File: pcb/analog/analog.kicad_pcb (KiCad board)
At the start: 2 copper layers, 70 x 70 mm, 65 parts, among them J1 USB_C_Receptacle_USB2.0, SW1 SW_Push, SW2 SW_Push, U1 SRV05-4, U2 XC6206P332MR, U3 DRV5056A3xDBZxQ1, U4 DRV5056A3xDBZxQ1, U5 DRV5056A3xDBZxQ1, U6 74AHCT1G125, U7 74AHCT1G125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

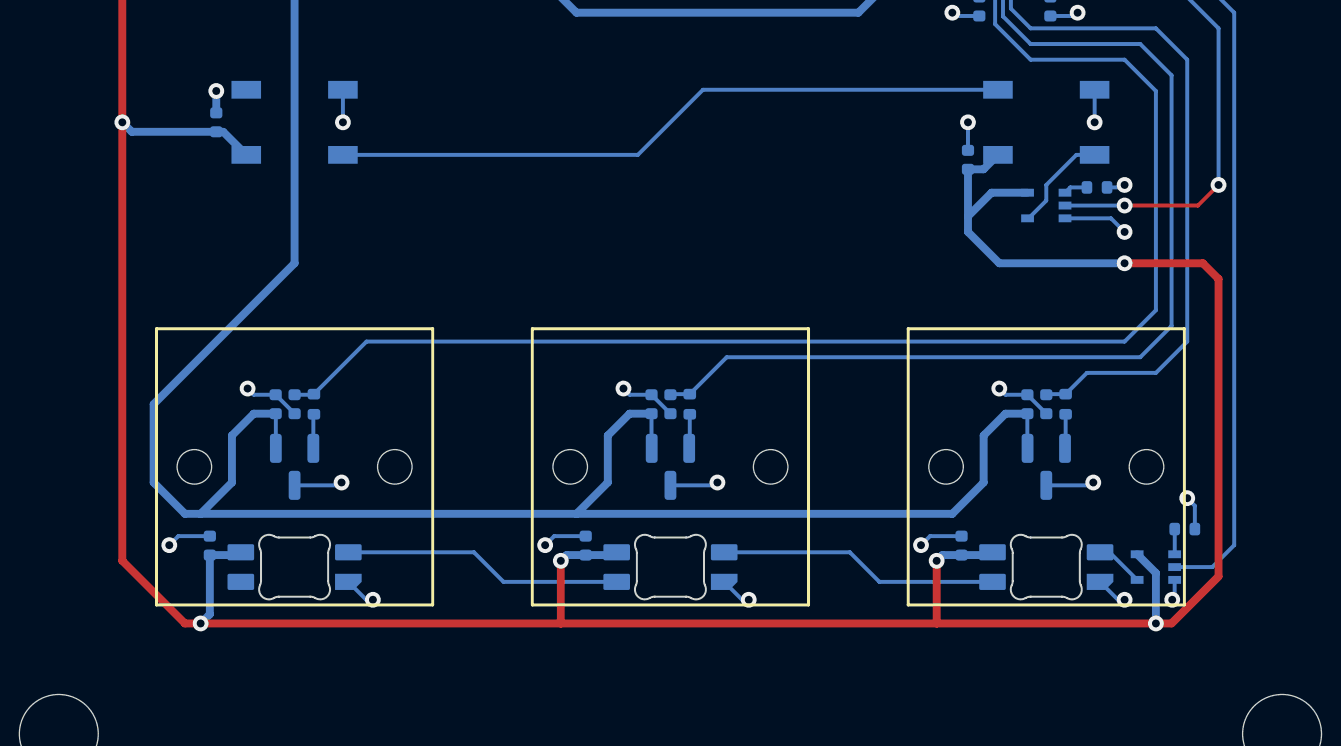
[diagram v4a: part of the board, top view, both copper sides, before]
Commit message: refactor: route +5v for underglow without crossing over analog lines
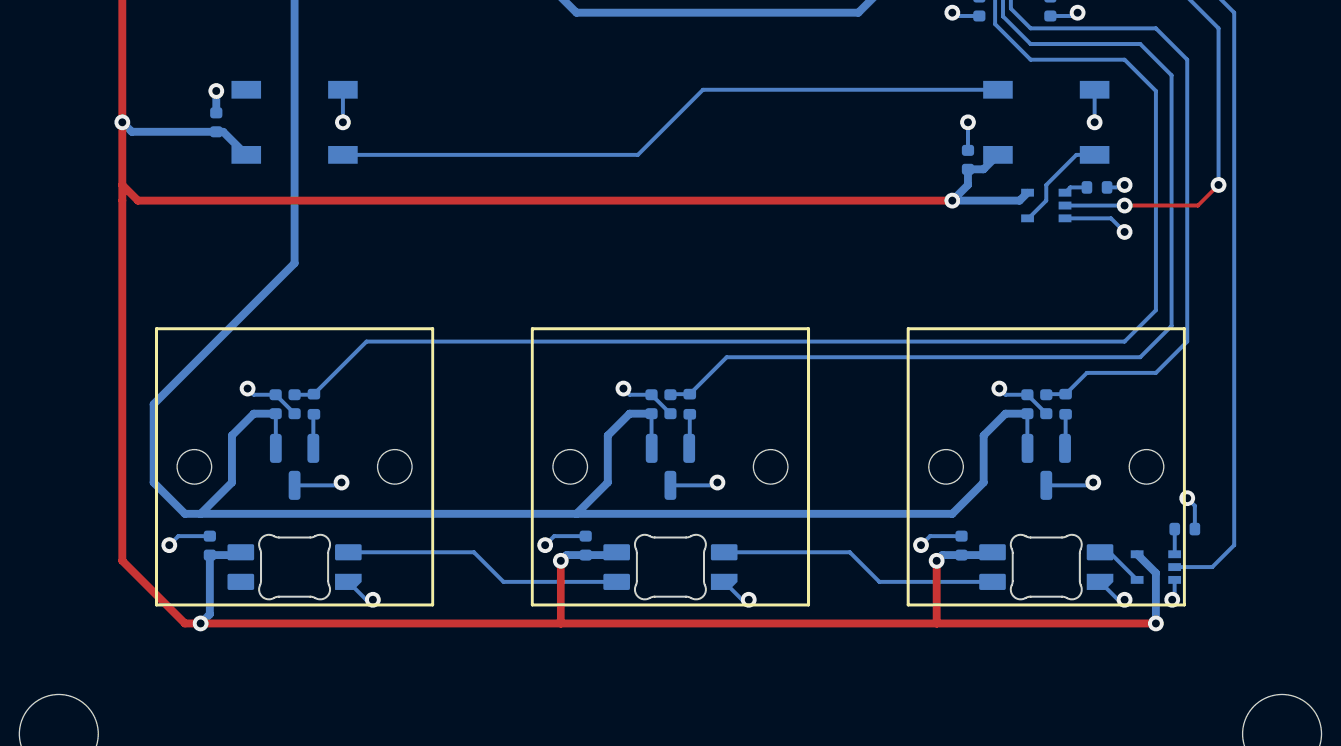
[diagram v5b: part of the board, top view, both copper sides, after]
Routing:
- net +5V: track 203.7 -> 212.3 mm
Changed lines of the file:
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@@
   (segment (start 76.670543 39.959446) (end 76.670543 40.93645) (width 0.2) (layer "B.Cu") (net 2))
   (segment (start 45.24375 76.2) (end 45.24375 73.025) (width 0.4) (layer "F.Cu") (net 3))
+  (segment (start 23.01875 54.76875) (end 23.01875 73.025) (width 0.4) (layer "F.Cu") (net 3))
   (segment (start 23.01875 29.36875) (end 23.01875 50.8) (width 0.4) (layer "F.Cu") (net 3))
-  (segment (start 23.01875 50.8) (end 23.01875 73.025) (width 0.4) (layer "F.Cu") (net 3))
-  (segment (start 77.7875 74.6125) (end 78.58125 73.81875) (width 0.4) (layer "F.Cu") (net 3))
   (segment (start 45.24375 76.2) (end 64.29375 76.2) (width 0.4) (layer "F.Cu") (net 3))
   (segment (start 23.01875 73.025) (end 26.19375 76.2) (width 0.4) (layer "F.Cu") (net 3))
   (segment (start 26.9875 76.2) (end 45.24375 76.2) (width 0.4) (layer "F.Cu") (net 3))
   (segment (start 26.19375 76.2) (end 26.9875 76.2) (width 0.4) (layer "F.Cu") (net 3))
+  (segment (start 23.01875 50.8) (end 23.01875 53.975) (width 0.4) (layer "F.Cu") (net 3))
   (segment (start 40.48125 25.4) (end 26.9875 25.4) (width 0.4) (layer "F.Cu") (net 3))
-  (segment (start 78.58125 73.81875) (end 78.58125 58.7375) (width 0.4) (layer "F.Cu") (net 3))
-  (segment (start 75.40625 76.2) (end 76.2 76.2) (width 0.4) (layer "F.Cu") (net 3))
-  (segment (start 77.7875 57.94375) (end 73.81875 57.94375) (width 0.4) (layer "F.Cu") (net 3))
+  (segment (start 23.8125 54.76875) (end 65.0875 54.76875) (width 0.4) (layer "F.Cu") (net 3))
+  (segment (start 23.01875 53.975) (end 23.01875 54.76875) (width 0.4) (layer "F.Cu") (net 3))
   (segment (start 26.9875 25.4) (end 23.01875 29.36875) (width 0.4) (layer "F.Cu") (net 3))
   (segment (start 64.29375 76.2) (end 75.40625 76.2) (width 0.4) (layer "F.Cu") (net 3))
-  (segment (start 76.2 76.2) (end 77.7875 74.6125) (width 0.4) (layer "F.Cu") (net 3))
+  (segment (start 23.01875 53.975) (end 23.8125 54.76875) (width 0.4) (layer "F.Cu") (net 3))
   (segment (start 64.29375 76.2) (end 64.29375 73.025) (width 0.4) (layer "F.Cu") (net 3))
-  (segment (start 78.58125 58.7375) (end 77.7875 57.94375) (width 0.4) (layer "F.Cu") (net 3))
   (via (at 45.24375 73.025) (size 0.8) (drill 0.4) (layers "F.Cu" "B.Cu") (net 3))
   (via (at 23.01875 50.8) (size 0.8) (drill 0.4) (layers "F.Cu" "B.Cu") (net 3))
   (via (at 26.9875 76.2) (size 0.8) (drill 0.4) (layers "F.Cu" "B.Cu") (net 3))
+  (via (at 65.0875 54.76875) (size 0.8) (drill 0.4) (layers "F.Cu" "B.Cu") (net 3))
   (via (at 40.48125 25.4) (size 0.8) (drill 0.4) (layers "F.Cu" "B.Cu") (net 3))
   (via (at 75.40625 76.2) (size 0.8) (drill 0.4) (layers "F.Cu" "B.Cu") (net 3))
   (via (at 64.29375 73.025) (size 0.8) (drill 0.4) (layers "F.Cu" "B.Cu") (net 3))
-  (via (at 73.81875 57.94375) (size 0.8) (drill 0.4) (layers "F.Cu" "B.Cu") (net 3))
-  (segment (start 67.076648 54.367102) (end 65.88125 55.5625) (width 0.4) (layer "B.Cu") (net 3))
-  (segment (start 65.88125 55.5625) (end 65.88125 53.18125) (width 0.4) (layer "B.Cu") (net 3))
+  (segment (start 68.9 54.367102) (end 68.498352 54.76875) (width 0.4) (layer "B.Cu") (net 3))
+  (segment (start 65.88125 53.18125) (end 65.88125 53.975) (width 0.4) (layer "B.Cu") (net 3))
   (segment (start 46.0375 29.36875) (end 44.30625 27.6375) (width 0.4) (layer "B.Cu") (net 3))
   (segment (start 23.01875 50.8) (end 23.49875 51.28) (width 0.4) (layer "B.Cu") (net 3))
@@
   (segment (start 65.555346 72.733806) (end 66.983694 72.733806) (width 0.4) (layer "B.Cu") (net 3))
   (segment (start 65.88125 53.18125) (end 66.66875 53.18125) (width 0.4) (layer "B.Cu") (net 3))
-  (segment (start 73.81875 57.94375) (end 67.46875 57.94375) (width 0.4) (layer "B.Cu") (net 3))
-  (segment (start 67.46875 57.94375) (end 65.88125 56.35625) (width 0.4) (layer "B.Cu") (net 3))
   (segment (start 27.455346 72.733806) (end 28.883694 72.733806) (width 0.4) (layer "B.Cu") (net 3))
   (segment (start 64.584944 72.733806) (end 64.29375 73.025) (width 0.4) (layer "B.Cu") (net 3))
   (segment (start 75.40625 76.2) (end 75.40625 73.6425) (width 0.4) (layer "B.Cu") (net 3))
+  (segment (start 65.88125 53.975) (end 65.0875 54.76875) (width 0.4) (layer "B.Cu") (net 3))
   (segment (start 44.309018 31.097232) (end 44.309018 32.2) (width 0.4) (layer "B.Cu") (net 3))
   (segment (start 28.13 51.28) (end 29.3 52.45) (width 0.4) (layer "B.Cu") (net 3))
@@
   (segment (start 26.9875 76.2) (end 27.455346 75.732154) (width 0.4) (layer "B.Cu") (net 3))
   (segment (start 44.30625 32.202768) (end 44.309018 32.2) (width 0.4) (layer "B.Cu") (net 3))
+  (segment (start 68.498352 54.76875) (end 65.0875 54.76875) (width 0.4) (layer "B.Cu") (net 3))
   (segment (start 66.983694 72.733806) (end 67.125 72.5925) (width 0.4) (layer "B.Cu") (net 3))
-  (segment (start 65.88125 56.35625) (end 65.88125 55.5625) (width 0.4) (layer "B.Cu") (net 3))
   (segment (start 46.0375 29.36875) (end 44.309018 31.097232) (width 0.4) (layer "B.Cu") (net 3))
   (segment (start 45.24375 73.025) (end 45.534944 72.733806) (width 0.4) (layer "B.Cu") (net 3))
-  (segment (start 68.9 54.367102) (end 67.076648 54.367102) (width 0.4) (layer "B.Cu") (net 3))
   (segment (start 44.30625 33.7875) (end 44.30625 32.202768) (width 0.4) (layer "B.Cu") (net 3))
   (segment (start 66.66875 53.18125) (end 67.4 52.45) (width 0.4) (layer "B.Cu") (net 3))

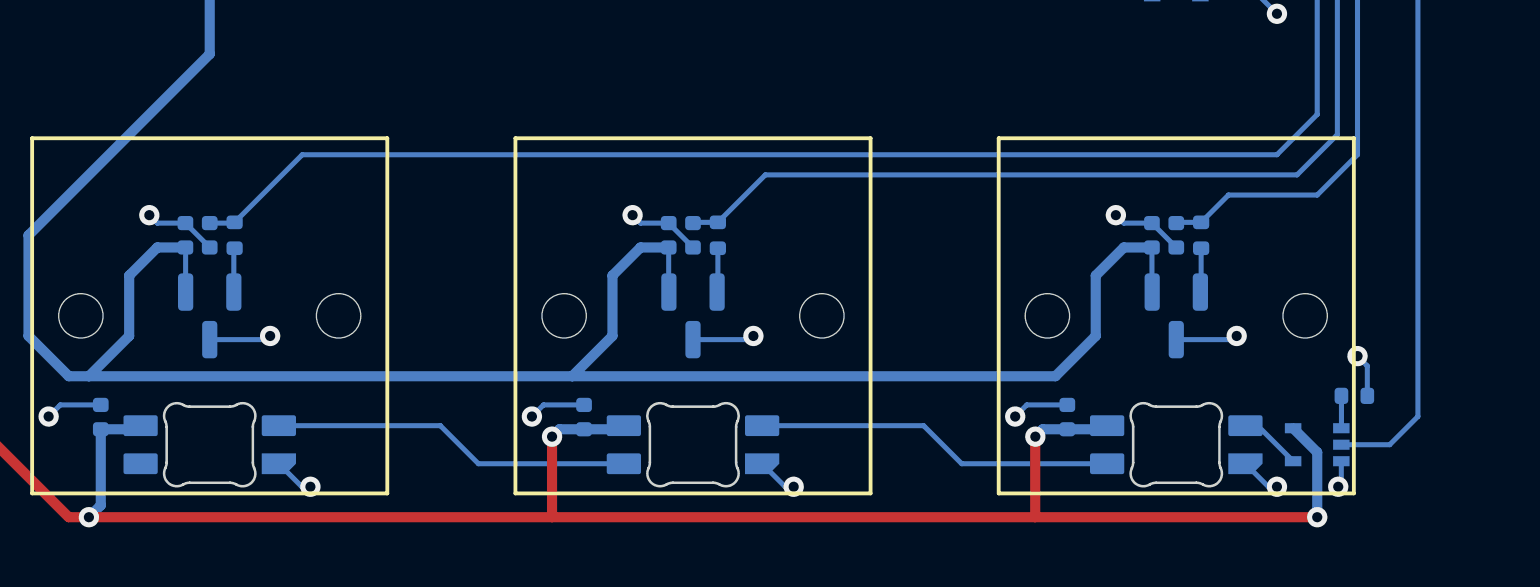
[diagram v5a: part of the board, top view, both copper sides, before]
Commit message: fix: resolve silkscreenm overlaps in keyswitch area
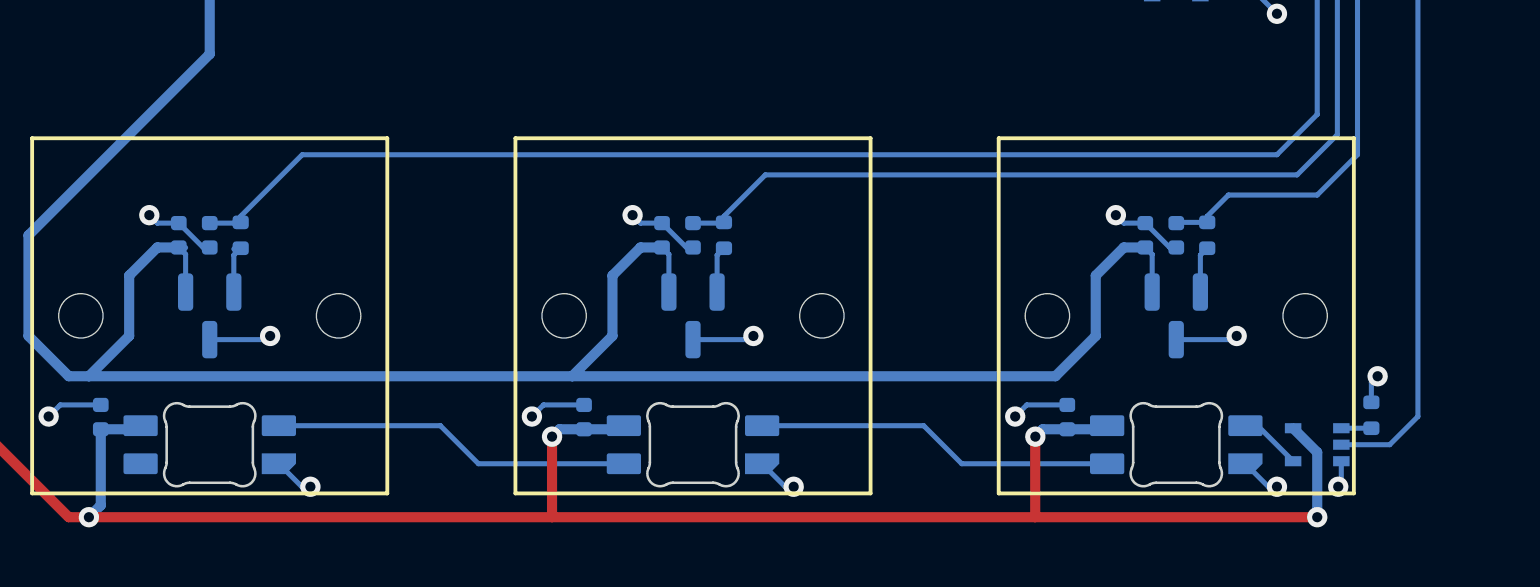
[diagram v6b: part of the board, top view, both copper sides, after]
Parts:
- moved R6 1.02 mm to (77.5, 72.2), turned to 90 degrees
- moved C1 0.26 mm to (68.6, 65.1)
- moved C2 0.26 mm to (49.6, 65.1)
- moved C3 0.26 mm to (30.5, 65.1)
- moved R5 0.24 mm to (33.0, 65.1)
- moved R3 0.24 mm to (71.1, 65.1)
- moved R4 0.24 mm to (52.0, 65.1)
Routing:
- net GND: track 122.6 -> 122.0 mm
